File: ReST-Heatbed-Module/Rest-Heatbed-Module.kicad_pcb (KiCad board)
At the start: 2 copper layers, 31 x 49.2 mm, 19 parts, among them P1 02-SCREW-TERM, P2 02X04-MALE, P3 02-SCREW-TERM, P4 01X02-MALE, P5 02-SCREW-TERM, Q1 Q_BSH105, Q2 Q_AOT240L

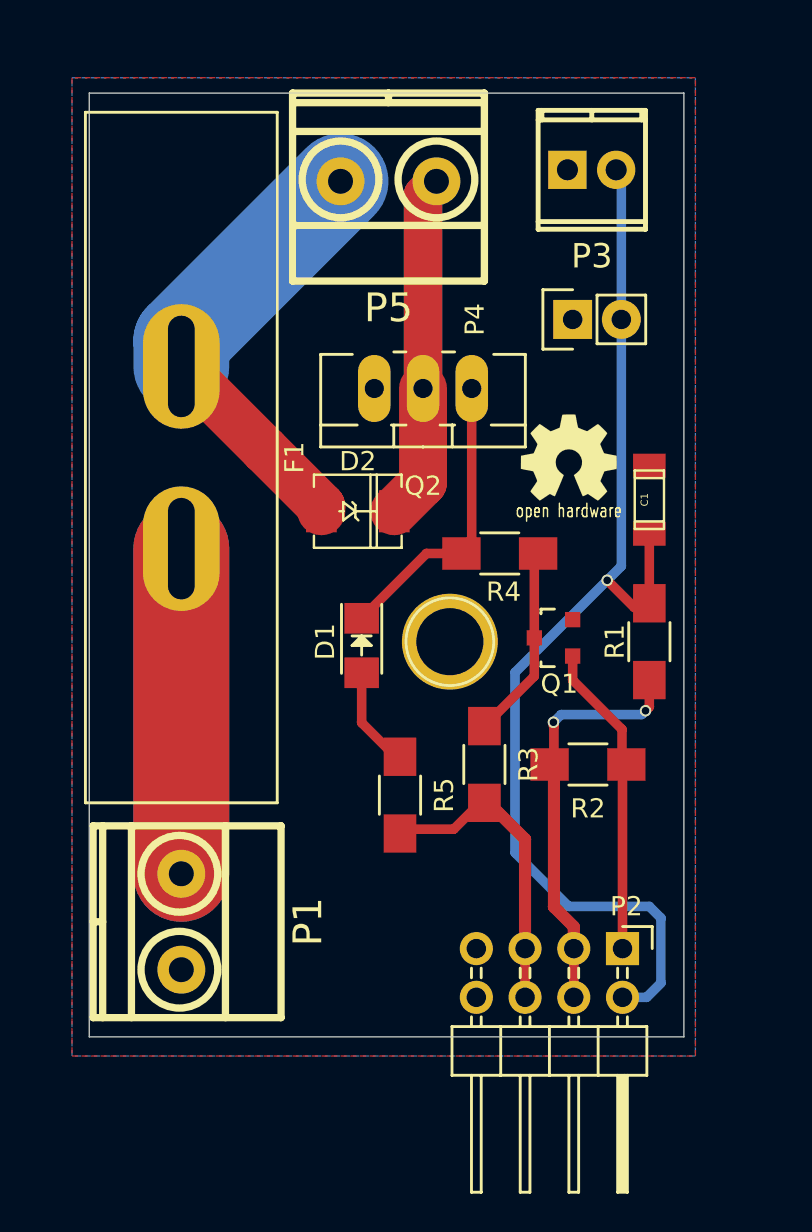
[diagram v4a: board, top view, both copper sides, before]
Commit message: Finally removed all unnecessary Libs and added Heatsink for 5V Regulator
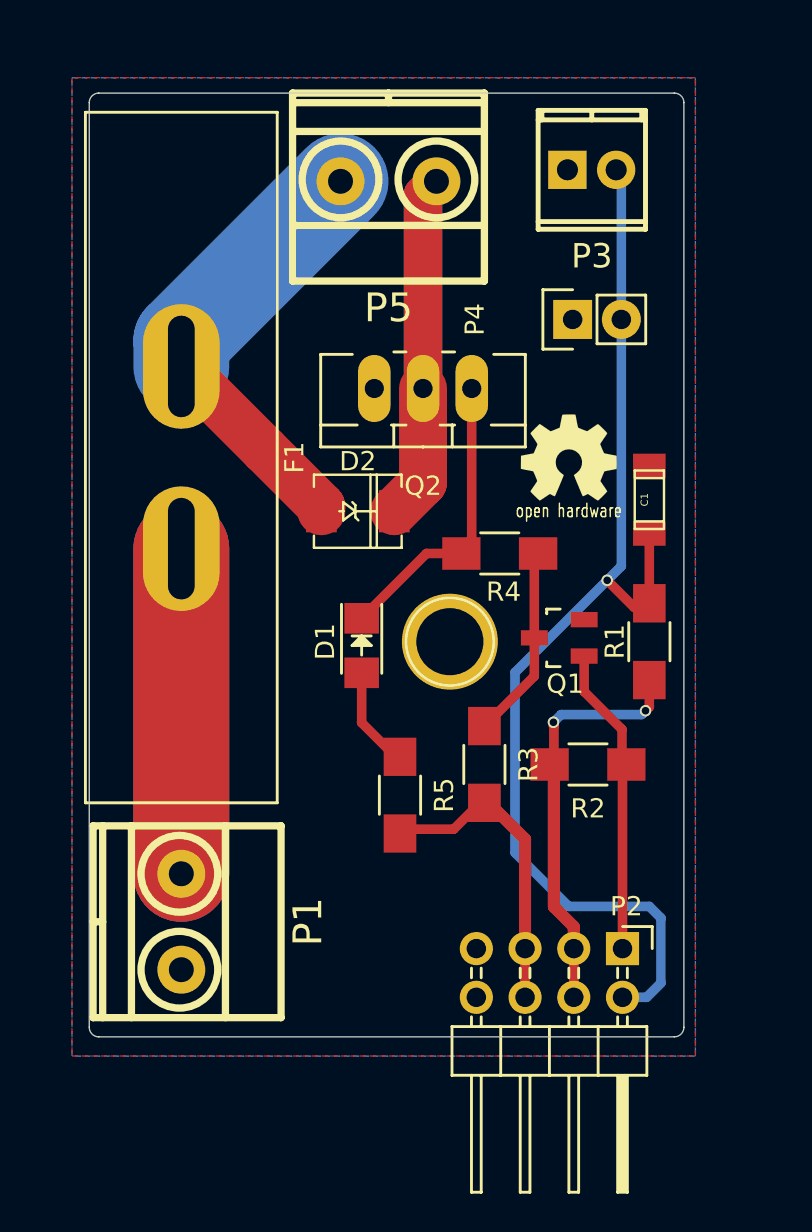
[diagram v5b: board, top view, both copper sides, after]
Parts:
- Q1: footprint TO_SOT_Packages_SMD:SOT-23 -> ReST-Library:SOT-23
- moved Q1 0.30 mm to (136.7, 133.8)
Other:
- outline, holes or cut-outs redrawn
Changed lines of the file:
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@@
     (links 29)
     (no_connects 0)
-    (area 112.194999 105.394999 143.205001 154.605001)
+    (area 109.4 102.4 148.803543 163.425001)
     (thickness 1.6)
-    (drawings 6)
+    (drawings 10)
     (tracks 69)
     (zones 0)
@@
     (trace_min 0.2)
     (segment_width 0.2)
-    (edge_width 0.15)
+    (edge_width 0.01)
     (via_size 0.6)
     (via_drill 0.4)
@@
     )
     (model ../../../../../../Users/Matjas/Documents/Git/RepRapSTM32duinoDriver/3D-Models/conn_mkds/mkds_1,5-2.wrl
-      (at (xyz 0 0 0))
-      (scale (xyz 1 1 1))
-      (rotate (xyz 0 0 0))
-    )
-  )
-  (module TO_SOT_Packages_SMD:SOT-23 (layer F.Cu)
-    (at 136.4 133.8 90)
-    (descr "SOT-23, Standard")
-    (tags SOT-23)
-    (attr smd)
-    (fp_text reference Q1 (at -2.4 0.3 180) (layer F.SilkS)
-      (effects (font (size 1 1) (thickness 0.15)))
-    )
-    (fp_text value Q_BSH105 (at 0 2.3 90) (layer F.Fab)
-      (effects (font (size 1 1) (thickness 0.15)))
-    )
-    (fp_line (start -1.65 -1.6) (end 1.65 -1.6) (layer F.CrtYd) (width 0.05))
-    (fp_line (start 1.65 -1.6) (end 1.65 1.6) (layer F.CrtYd) (width 0.05))
-    (fp_line (start 1.65 1.6) (end -1.65 1.6) (layer F.CrtYd) (width 0.05))
-    (fp_line (start -1.65 1.6) (end -1.65 -1.6) (layer F.CrtYd) (width 0.05))
-    (fp_line (start 1.29916 -0.65024) (end 1.2509 -0.65024) (layer F.SilkS) (width 0.15))
-    (fp_line (start -1.49982 0.0508) (end -1.49982 -0.65024) (layer F.SilkS) (width 0.15))
-    (fp_line (start -1.49982 -0.65024) (end -1.2509 -0.65024) (layer F.SilkS) (width 0.15))
-    (fp_line (start 1.29916 -0.65024) (end 1.49982 -0.65024) (layer F.SilkS) (width 0.15))
-    (fp_line (start 1.49982 -0.65024) (end 1.49982 0.0508) (layer F.SilkS) (width 0.15))
-    (pad 1 smd rect (at -0.95 1.00076 90) (size 0.8001 0.8001) (layers F.Cu F.Paste F.Mask)
-      (net 10 /PWM-HEATBED))
-    (pad 2 smd rect (at 0.95 1.00076 90) (size 0.8001 0.8001) (layers F.Cu F.Paste F.Mask)
-      (net 2 GND))
-    (pad 3 smd rect (at 0 -0.99822 90) (size 0.8001 0.8001) (layers F.Cu F.Paste F.Mask)
-      (net 11 "Net-(Q1-Pad3)"))
-    (model TO_SOT_Packages_SMD.3dshapes/SOT-23.wrl
       (at (xyz 0 0 0))
       (scale (xyz 1 1 1))
@@
     (pad 1 thru_hole circle (at 0 0) (size 5 5) (drill 3.5) (layers *.Cu *.Mask F.SilkS))
   )
+  (module ReST-Library:SOT-23 (layer F.Cu)
+    (at 136.7 133.8 90)
+    (descr "SOT-23, Standard")
+    (tags SOT-23)
+    (attr smd)
+    (fp_text reference Q1 (at -2.4 0.3 180) (layer F.SilkS)
+      (effects (font (size 1 1) (thickness 0.15)))
+    )
+    (fp_text value Q_BSH105 (at 0 2.3 90) (layer F.Fab)
+      (effects (font (size 1 1) (thickness 0.15)))
+    )
+    (fp_line (start -1.65 -1.6) (end 1.65 -1.6) (layer F.CrtYd) (width 0.05))
+    (fp_line (start 1.65 -1.6) (end 1.65 1.6) (layer F.CrtYd) (width 0.05))
+    (fp_line (start 1.65 1.6) (end -1.65 1.6) (layer F.CrtYd) (width 0.05))
+    (fp_line (start -1.65 1.6) (end -1.65 -1.6) (layer F.CrtYd) (width 0.05))
+    (fp_line (start 1.29916 -0.65024) (end 1.2509 -0.65024) (layer F.SilkS) (width 0.15))
+    (fp_line (start -1.49982 0.0508) (end -1.49982 -0.65024) (layer F.SilkS) (width 0.15))
+    (fp_line (start -1.49982 -0.65024) (end -1.2509 -0.65024) (layer F.SilkS) (width 0.15))
+    (fp_line (start 1.29916 -0.65024) (end 1.49982 -0.65024) (layer F.SilkS) (width 0.15))
+    (fp_line (start 1.49982 -0.65024) (end 1.49982 0.0508) (layer F.SilkS) (width 0.15))
+    (pad 1 smd rect (at -0.95 1.3 90) (size 0.8001 1.4) (layers F.Cu F.Paste F.Mask)
+      (net 10 /PWM-HEATBED))
+    (pad 2 smd rect (at 0.95 1.3 90) (size 0.8001 1.4) (layers F.Cu F.Paste F.Mask)
+      (net 2 GND))
+    (pad 3 smd rect (at 0 -1.3 90) (size 0.8001 1.4) (layers F.Cu F.Paste F.Mask)
+      (net 11 "Net-(Q1-Pad3)"))
+    (model TO_SOT_Packages_SMD.3dshapes/SOT-23.wrl
+      (at (xyz 0 0 0))
+      (scale (xyz 1 1 1))
+      (rotate (xyz 0 0 0))
+    )
+  )
+  (gr_arc (start 142.7 154.1) (end 143.2 154.1) (angle 90) (layer Edge.Cuts) (width 0.01))
+  (gr_arc (start 112.7 154.1) (end 112.7 154.6) (angle 90) (layer Edge.Cuts) (width 0.01))
+  (gr_arc (start 112.7 105.9) (end 112.2 105.9) (angle 90) (layer Edge.Cuts) (width 0.01))
+  (gr_arc (start 142.7 105.9) (end 142.7 105.4) (angle 90) (layer Edge.Cuts) (width 0.01))
+  (gr_line (start 112.7 105.4) (end 142.7 105.4) (angle 90) (layer Edge.Cuts) (width 0.01))
+  (gr_line (start 112.2 154.1) (end 112.2 105.9) (angle 90) (layer Edge.Cuts) (width 0.01))
+  (gr_line (start 142.7 154.6) (end 112.7 154.6) (angle 90) (layer Edge.Cuts) (width 0.01))
+  (gr_line (start 143.2 105.9) (end 143.2 154.1) (angle 90) (layer Edge.Cuts) (width 0.01))
   (gr_text "by Straw" (at 129.5 138.2) (layer B.SilkS)
     (effects (font (size 1 1) (thickness 0.2)) (justify mirror))
@@
     (effects (font (size 1.5 1.5) (thickness 0.2)) (justify mirror))
   )
-  (gr_line (start 112.2 105.4) (end 143.2 105.4) (angle 90) (layer Edge.Cuts) (width 0.01))
-  (gr_line (start 112.2 154.6) (end 112.2 105.4) (angle 90) (layer Edge.Cuts) (width 0.01))
-  (gr_line (start 143.2 154.6) (end 112.2 154.6) (angle 90) (layer Edge.Cuts) (width 0.01))
-  (gr_line (start 143.2 154.6) (end 143.2 105.4) (angle 90) (layer Edge.Cuts) (width 0.01))
   (segment (start 139.94 117.2) (end 139.94 109.67) (width 0.5) (layer B.Cu) (net 1))
   (segment (start 139.94 109.67) (end 139.67 109.4) (width 0.5) (layer B.Cu) (net 1))
@@
   (segment (start 136.42454 147.82454) (end 137.46 148.86) (width 0.635) (layer F.Cu) (net 9))
   (segment (start 137.46 152.54) (end 137.46 152.46) (width 0.25) (layer F.Cu) (net 9))
+  (segment (start 138 136.6) (end 138 134.75) (width 0.5) (layer F.Cu) (net 10))
+  (segment (start 139.97546 138.57546) (end 138 136.6) (width 0.5) (layer F.Cu) (net 10))
   (segment (start 139.97546 140.4) (end 139.97546 138.57546) (width 0.5) (layer F.Cu) (net 10))
-  (segment (start 139.97546 138.57546) (end 137.40076 136.00076) (width 0.5) (layer F.Cu) (net 10))
-  (segment (start 137.40076 136.00076) (end 137.40076 134.75) (width 0.5) (layer F.Cu) (net 10))
   (segment (start 140 150) (end 140 140.42454) (width 0.5) (layer F.Cu) (net 10))
   (segment (start 140 140.42454) (end 139.97546 140.4) (width 0.5) (layer F.Cu) (net 10))

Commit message: Added IRLML2502 Module and added Ground vias everywhere
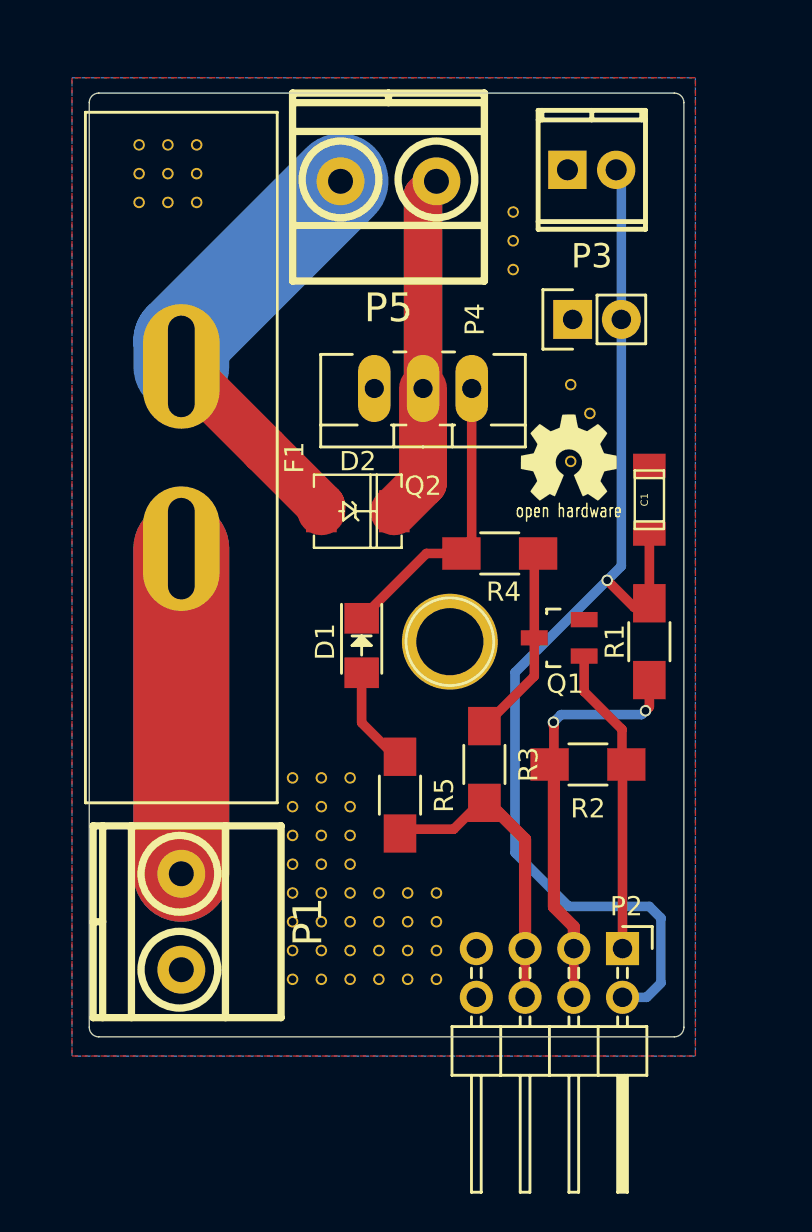
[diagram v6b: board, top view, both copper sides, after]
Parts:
- added 1111: , ReST-Library:VIA-0.6mm, F.Cu at (122.8, 141.1)
- added 11111: , ReST-Library:VIA-0.6mm, F.Cu at (134.3, 111.6)
- added 111111: , ReST-Library:VIA-0.6mm, F.Cu at (137.3, 120.6)
- added 111111: , ReST-Library:VIA-0.6mm, F.Cu at (114.8, 108.1)
- added 1111111: , ReST-Library:VIA-0.6mm, F.Cu at (127.3, 147.1)
- added 1111112: , ReST-Library:VIA-0.6mm, F.Cu at (127.3, 148.6)
- added 1111113: , ReST-Library:VIA-0.6mm, F.Cu at (127.3, 150.1)
- added 1111114: , ReST-Library:VIA-0.6mm, F.Cu at (127.3, 151.6)
- added 111112: , ReST-Library:VIA-0.6mm, F.Cu at (138.3, 122.1)
- added 111112: , ReST-Library:VIA-0.6mm, F.Cu at (114.8, 109.6)
- added 1111121: , ReST-Library:VIA-0.6mm, F.Cu at (128.8, 147.1)
- added 1111122: , ReST-Library:VIA-0.6mm, F.Cu at (128.8, 148.6)
- added 1111123: , ReST-Library:VIA-0.6mm, F.Cu at (128.8, 150.1)
- added 1111124: , ReST-Library:VIA-0.6mm, F.Cu at (128.8, 151.6)
- added 111113: , ReST-Library:VIA-0.6mm, F.Cu at (137.3, 124.6)
- added 111113: , ReST-Library:VIA-0.6mm, F.Cu at (114.8, 111.1)
- added 1111131: , ReST-Library:VIA-0.6mm, F.Cu at (130.3, 147.1)
- added 1111132: , ReST-Library:VIA-0.6mm, F.Cu at (130.3, 148.6)
- added 1111133: , ReST-Library:VIA-0.6mm, F.Cu at (130.3, 150.1)
- added 1111134: , ReST-Library:VIA-0.6mm, F.Cu at (130.3, 151.6)
- added 11112: , ReST-Library:VIA-0.6mm, F.Cu at (134.3, 113.1)
- added 111121: , ReST-Library:VIA-0.6mm, F.Cu at (116.3, 108.1)
- added 111122: , ReST-Library:VIA-0.6mm, F.Cu at (116.3, 109.6)
- added 111123: , ReST-Library:VIA-0.6mm, F.Cu at (116.3, 111.1)
- added 11113: , ReST-Library:VIA-0.6mm, F.Cu at (134.3, 114.6)
- added 111131: , ReST-Library:VIA-0.6mm, F.Cu at (117.8, 108.1)
- added 111132: , ReST-Library:VIA-0.6mm, F.Cu at (117.8, 109.6)
- added 111133: , ReST-Library:VIA-0.6mm, F.Cu at (117.8, 111.1)
- added 1112: , ReST-Library:VIA-0.6mm, F.Cu at (122.8, 142.6)
- added 1113: , ReST-Library:VIA-0.6mm, F.Cu at (122.8, 144.1)
- added 1114: , ReST-Library:VIA-0.6mm, F.Cu at (122.8, 145.6)
- added 1115: , ReST-Library:VIA-0.6mm, F.Cu at (122.8, 147.1)
- added 1116: , ReST-Library:VIA-0.6mm, F.Cu at (122.8, 148.6)
- added 1117: , ReST-Library:VIA-0.6mm, F.Cu at (122.8, 150.1)
- added 1118: , ReST-Library:VIA-0.6mm, F.Cu at (122.8, 151.6)
- added 1121: , ReST-Library:VIA-0.6mm, F.Cu at (124.3, 141.1)
- added 1122: , ReST-Library:VIA-0.6mm, F.Cu at (124.3, 142.6)
- added 1123: , ReST-Library:VIA-0.6mm, F.Cu at (124.3, 144.1)
- added 1124: , ReST-Library:VIA-0.6mm, F.Cu at (124.3, 145.6)
- added 1125: , ReST-Library:VIA-0.6mm, F.Cu at (124.3, 147.1)
- added 1126: , ReST-Library:VIA-0.6mm, F.Cu at (124.3, 148.6)
- added 1127: , ReST-Library:VIA-0.6mm, F.Cu at (124.3, 150.1)
- added 1128: , ReST-Library:VIA-0.6mm, F.Cu at (124.3, 151.6)
- added 1131: , ReST-Library:VIA-0.6mm, F.Cu at (125.8, 141.1)
- added 1132: , ReST-Library:VIA-0.6mm, F.Cu at (125.8, 142.6)
- added 1133: , ReST-Library:VIA-0.6mm, F.Cu at (125.8, 144.1)
- added 1134: , ReST-Library:VIA-0.6mm, F.Cu at (125.8, 145.6)
- added 1135: , ReST-Library:VIA-0.6mm, F.Cu at (125.8, 147.1)
- added 1136: , ReST-Library:VIA-0.6mm, F.Cu at (125.8, 148.6)
- added 1137: , ReST-Library:VIA-0.6mm, F.Cu at (125.8, 150.1)
- added 1138: , ReST-Library:VIA-0.6mm, F.Cu at (125.8, 151.6)

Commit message: Finished PCB design, notations and silkscreen
gonna work to finish a combined design for cheaper pcb cost and put
everything i need into the bom
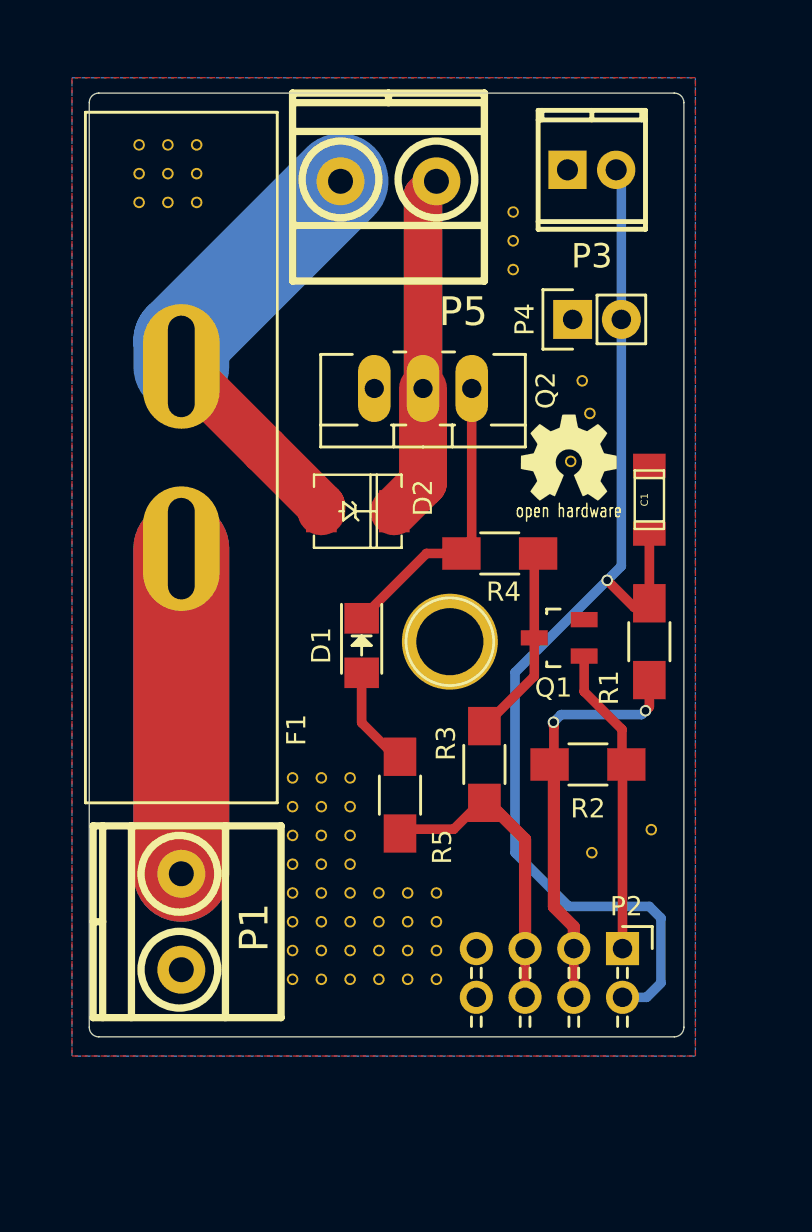
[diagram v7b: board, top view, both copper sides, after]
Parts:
- added ?: , ReST-Library:VIA-0.6mm, F.Cu at (138.4, 145.0)
- added ?: , ReST-Library:VIA-0.6mm, F.Cu at (141.5, 143.8)
- ? (x2): renamed from G***; value LOGO -> (none)
- ?: value 1pin -> (none)
- C1: value 10uF -> (none)
- D1: value LED -> (none)
- D2: value D_1N400x-SMD -> (none)
- F1: value 15A -> (none)
- P1, P3, P5: value 02-SCREW-TERM -> (none)
- P2: value 02X04-MALE -> (none); footprint Pin_Headers:Pin_Header_Angled_2x04 -> ReST-Library:Pin_Header_Angled_2x04
- P4: value 01X02-MALE -> (none)
- Q1: value Q_BSH105 -> (none)
- Q2: value Q_AOT240L -> (none)
- R1: value 4.7K -> (none)
- R2, R3: value 100K -> (none)
- R4: value 22R -> (none)
- R5: value 470R -> (none)
- moved ? 0.63 mm to (137.9, 120.4)
- renumbered 1111122 to ?, 1111112 to ?, 1111131 to ?, 1111121 to ?, 1111111 to ?, 111113 to ?, 111112 to ?, 111111 to ?, 111133 to ?, 111123 to ?, 111132 to ?, 111122 to ?, 111131 to ?, 111121 to ?, 11113 to ?, 11112 to ?, 11111 to ?, 1111134 to ?, 1138 to ?, 1128 to ?, 1118 to ?, 1137 to ?, 1127 to ?, 1117 to ?, 1136 to ?, 1126 to ?, 1116 to ?, 1135 to ?, 1111124 to ?, 1125 to ?, 1115 to ?, 1134 to ?, 1124 to ?, 1114 to ?, 1133 to ?, 1123 to ?, 1113 to ?, 1132 to ?, 1122 to ?, 1111114 to ?, 1112 to ?, 1131 to ?, 1121 to ?, 1111 to ?, 1111133 to ?, 1111123 to ?, 1111113 to ?, 1111132 to ?
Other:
- board text added: "@maker_berry"
- board text removed: "by Straw"
